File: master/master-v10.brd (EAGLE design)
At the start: 47.9 x 59.7 mm, 41 parts, among them IC1 DS1820, IC2 DS3231/SO, J1 AVR_SPI_PRG_6PTH, U2 ATMEGA640/1280/2560-A, U3 FT232RL-BASICSSOP, U4 AP1117E, U5 USD-SOCKETNEW

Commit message: arrelado problema del ftdi
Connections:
- removed net VCCIO: U3.4
- new net N$24: C8.1, C9.1, JP1.VBUS, U3.20
- new net N$25: U3.17, U3.4
- net 3.3V: no longer C8.1, C9.1, U3.20
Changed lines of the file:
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@@
 </elements>
 <signals>
-<signal name="VCCIO">
-<contactref element="U3" pad="4"/>
-</signal>
 <signal name="GND" class="1">
 <contactref element="C1" pad="2"/>
@@
 <contactref element="R6" pad="2"/>
 <contactref element="R7" pad="2"/>
-<contactref element="U3" pad="20"/>
-<contactref element="C8" pad="1"/>
-<contactref element="C9" pad="1"/>
 <contactref element="U2" pad="10"/>
 <contactref element="U2" pad="31"/>
@@
 <contactref element="R10" pad="1"/>
 <contactref element="U5" pad="4"/>
-<wire x1="22.48" y1="38.33" x2="10.795" y2="57.94" width="0" layer="19" extent="1-1"/>
-<wire x1="24.48" y1="44.83" x2="22.48" y2="38.33" width="0" layer="19" extent="1-1"/>
-<wire x1="25.48" y1="44.83" x2="24.48" y2="44.83" width="0" layer="19" extent="1-1"/>
-<wire x1="34.48" y1="44.83" x2="25.48" y2="44.83" width="0" layer="19" extent="1-1"/>
+<wire x1="34.48" y1="44.83" x2="43.21" y2="51.775" width="0" layer="19" extent="1-1"/>
+<wire x1="25.48" y1="44.83" x2="34.48" y2="44.83" width="0" layer="19" extent="1-1"/>
+<wire x1="24.48" y1="44.83" x2="25.48" y2="44.83" width="0" layer="19" extent="1-1"/>
+<wire x1="22.48" y1="38.33" x2="24.48" y2="44.83" width="0" layer="19" extent="1-1"/>
 <wire x1="38.48" y1="35.83" x2="34.48" y2="44.83" width="0" layer="19" extent="1-1"/>
-<wire x1="8.1788" y1="29.21" x2="34.48" y2="44.83" width="0" layer="19" extent="1-1"/>
+<wire x1="26.98" y1="28.83" x2="22.48" y2="38.33" width="0" layer="19" extent="1-1"/>
+<wire x1="22.9362" y1="56.515" x2="24.48" y2="44.83" width="0" layer="19" extent="1-1"/>
+<wire x1="44.45" y1="25.4" x2="38.48" y2="35.83" width="0" layer="19" extent="1-1"/>
+<wire x1="10.795" y1="57.94" x2="22.9362" y2="56.515" width="0" layer="19" extent="1-1"/>
+<wire x1="13.97" y1="27.94" x2="26.98" y2="28.83" width="0" layer="19" extent="1-1"/>
+<wire x1="8.1788" y1="29.21" x2="13.97" y2="27.94" width="0" layer="19" extent="1-1"/>
 <wire x1="1.981" y1="29.21" x2="8.1788" y2="29.21" width="0" layer="19" extent="1-1"/>
-<wire x1="26.98" y1="28.83" x2="22.48" y2="38.33" width="0" layer="19" extent="1-1"/>
-<wire x1="28.5" y1="6.88" x2="38.48" y2="35.83" width="0" layer="19" extent="1-1"/>
-<wire x1="16.356" y1="15.535" x2="1.981" y2="29.21" width="0" layer="19" extent="1-1"/>
-<wire x1="22.9362" y1="56.515" x2="16.356" y2="15.535" width="0" layer="19" extent="1-1"/>
-<wire x1="-23.51" y1="69.85" x2="22.9362" y2="56.515" width="0" layer="19" extent="1-1"/>
+<wire x1="28.5" y1="6.88" x2="26.98" y2="28.83" width="0" layer="19" extent="1-1"/>
+<wire x1="-23.51" y1="69.85" x2="10.795" y2="57.94" width="0" layer="19" extent="1-1"/>
 <wire x1="-34.94" y1="69.85" x2="-23.51" y2="69.85" width="0" layer="19" extent="1-1"/>
 <wire x1="-38.75" y1="69.85" x2="-34.94" y2="69.85" width="0" layer="19" extent="1-1"/>
@@
 <wire x1="-48.88" y1="69.85" x2="-42.56" y2="69.85" width="0" layer="19" extent="1-1"/>
 <wire x1="-52.69" y1="69.85" x2="-48.88" y2="69.85" width="0" layer="19" extent="1-1"/>
-<wire x1="-48.49" y1="64.77" x2="-48.88" y2="69.85" width="0" layer="19" extent="1-1"/>
-<wire x1="-54.34" y1="63.5" x2="-48.49" y2="64.77" width="0" layer="19" extent="1-1"/>
-<wire x1="43.21" y1="51.775" x2="-54.34" y2="63.5" width="0" layer="19" extent="1-1"/>
-<wire x1="44.45" y1="25.4" x2="-38.75" y2="69.85" width="0" layer="19" extent="1-1"/>
-<wire x1="-42.23" y1="57.15" x2="44.45" y2="25.4" width="0" layer="19" extent="1-1"/>
+<wire x1="-42.23" y1="57.15" x2="-42.56" y2="69.85" width="0" layer="19" extent="1-1"/>
 <wire x1="-47.31" y1="57.15" x2="-42.23" y2="57.15" width="0" layer="19" extent="1-1"/>
-<wire x1="-65.42" y1="69.85" x2="43.21" y2="51.775" width="0" layer="19" extent="1-1"/>
-<wire x1="13.97" y1="27.94" x2="24.48" y2="44.83" width="0" layer="19" extent="1-1"/>
+<wire x1="-65.42" y1="69.85" x2="-52.69" y2="69.85" width="0" layer="19" extent="1-1"/>
 </signal>
 <signal name="N$6">
@@
 <wire x1="-13.97" y1="62.45" x2="-14.59" y2="73.66" width="0" layer="19" extent="1-1"/>
 </signal>
+<signal name="N$24">
+<contactref element="U3" pad="20"/>
+<contactref element="C8" pad="1"/>
+<contactref element="C9" pad="1"/>
+<contactref element="JP1" pad="VBUS"/>
+<wire x1="11.1" y1="8.91" x2="16.356" y2="15.535" width="0" layer="19" extent="1-1"/>
+<wire x1="-48.49" y1="64.77" x2="16.356" y2="15.535" width="0" layer="19" extent="1-1"/>
+<wire x1="-54.34" y1="63.5" x2="-48.49" y2="64.77" width="0" layer="19" extent="1-1"/>
+</signal>
+<signal name="N$25">
+<contactref element="U3" pad="17"/>
+<contactref element="U3" pad="4"/>
+<wire x1="9.044" y1="18.785" x2="16.356" y2="13.585" width="0" layer="19" extent="1-1"/>
+</signal>
 </signals>

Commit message: avanzado temperatura y otros
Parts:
- removed IC1: DS1820, DS1820:TO-92
- added J2: TWIG-2.0-DIPD, Grove :2.0_1X4_90
- added R13: 82k, SparkFun:0402-RES
- added R14, R16: 10k, SparkFun:0402-RES
- added R15: 3.3k, SparkFun:0402-RES
- added U6: INA169, SparkFun-AnalogIC:SOT23-5
- R10: value 4k7 -> 10k
- U1: value (none) -> MCP9804; device microbuilder:SOT23-8 -> MCP9804:MSOP8
- moved U1 162.6 mm to (-106.7, -15.2), turned to 0 degrees
- moved C7 100.4 mm to (-100.3, -8.89)
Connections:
- removed net CS: U2.19, U5.2
- removed net N$14: U2.12
- removed net N$2: U2.13
- removed net SCL: IC2.16, U1.5
- removed net SDA: IC2.15, U1.6
- removed net TEMP: IC1.2, R10.2
- new net CS_SD: U2.95, U5.2
- new net N$27: U1.6
- new net RX_GPS: J2.2, U2.13
- new net SENSOR_CURRENT: C7.1, R13.2, U2.97, U6.1
- new net SENSOR_VOLT: R14.2, R15.2, U2.96
- new net TX_GPS: J2.3, U2.12
- net 3.3V: now also J2.4, R16.1, U1.8, U6.5; no longer C7.1, IC1.3, U1.4
- net GND: now also J2.1, R13.1, R15.1, U1.4, U1.5, U6.2; no longer IC1.1, U1.3, U1.8
- net MOSI: now also IC2.15, R16.2, U1.1
- net RAW: now also R14.1
- net SCK: now also IC2.16, R10.2, U1.2
- net VIN+: now also U6.3; no longer U1.1
- net VIN-: now also U6.4; no longer U1.2

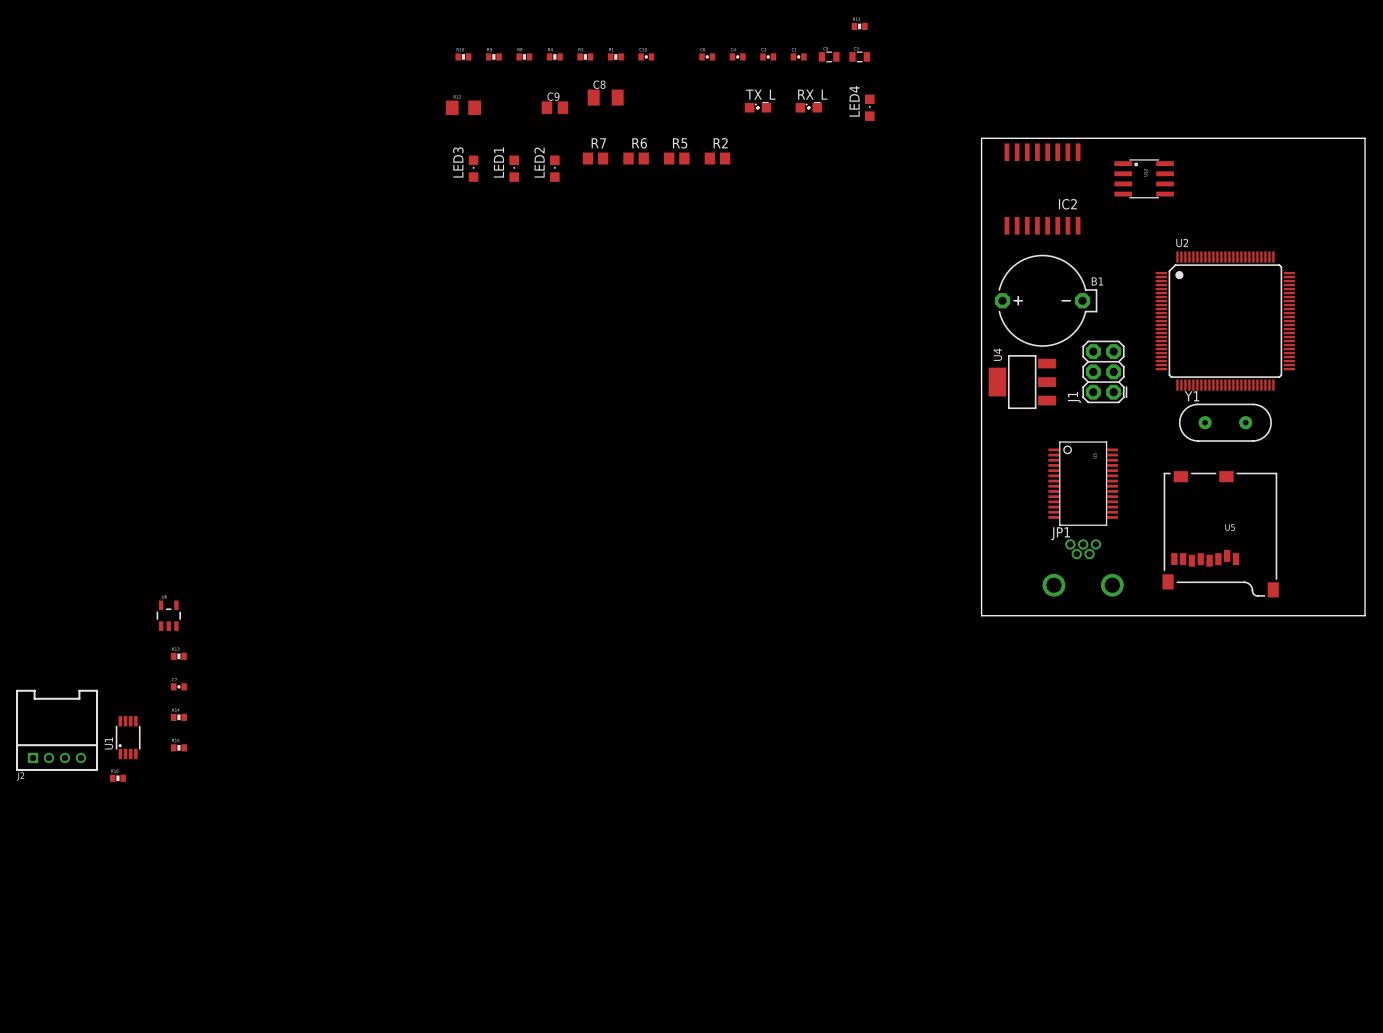
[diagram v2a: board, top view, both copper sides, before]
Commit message: agregado comunicacion
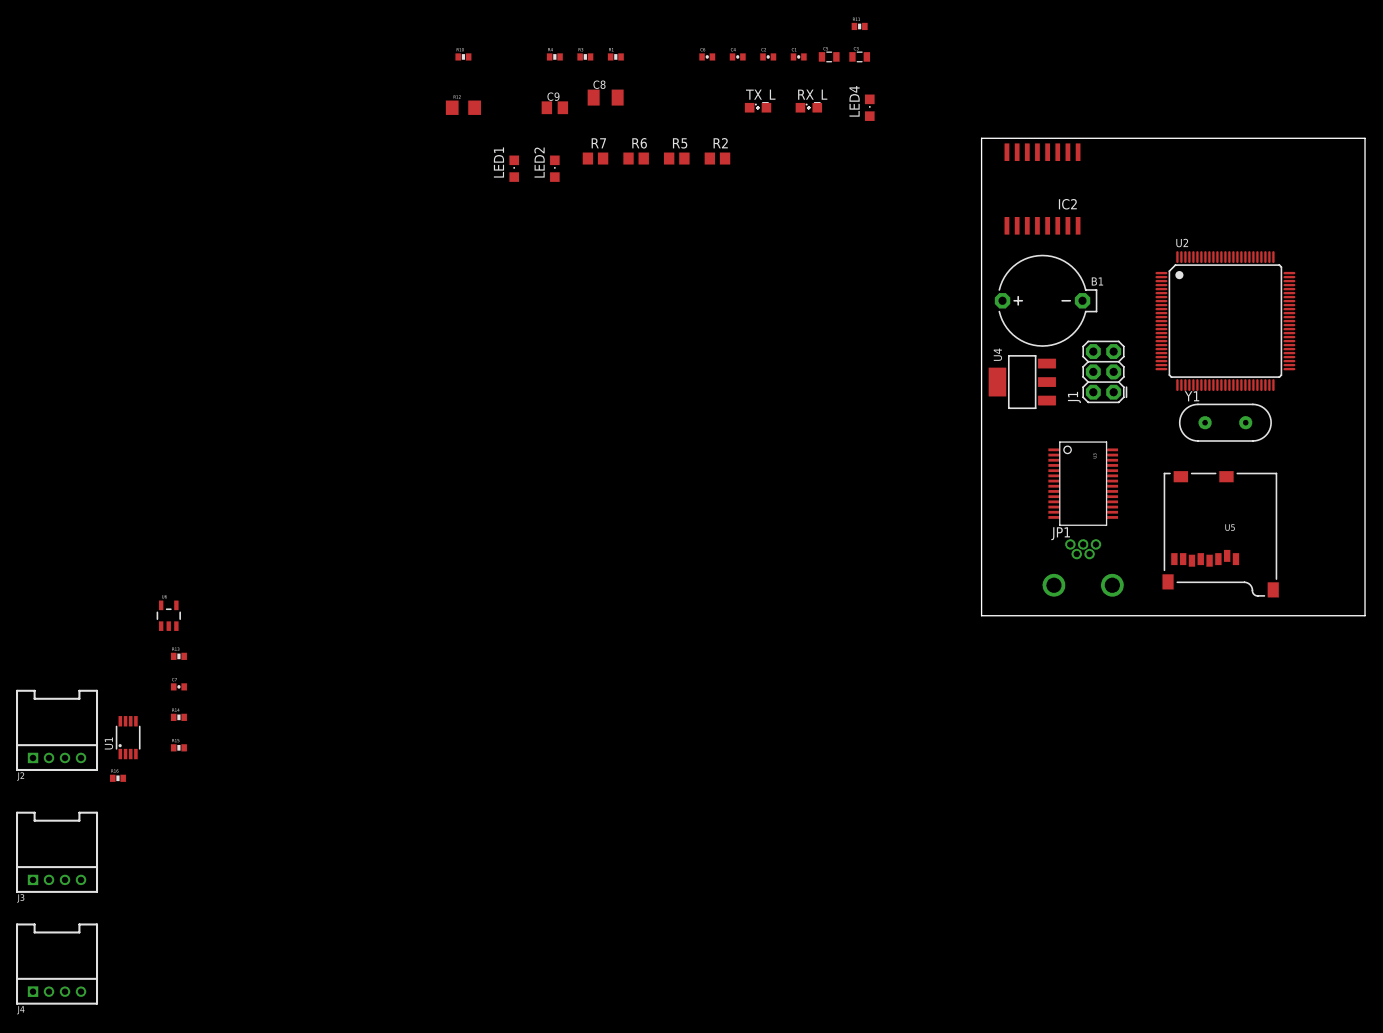
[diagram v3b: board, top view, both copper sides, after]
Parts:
- removed C10: 0.1uF, SparkFun:0402-CAP
- removed LED3: (no value), adafruit:CHIPLED_0805
- removed R8: 220, SparkFun:0402-RES
- removed R9: 1K, SparkFun:0402-RES
- removed U$2: RS485SOIC, SparkFun-DigitalIC:SO08
- added J3, J4: TWIG-2.0-DIPD, Grove :2.0_1X4_90
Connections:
- removed net A: R8.2, U$2.6
- removed net B: R8.1, U$2.7
- removed net N$15: U2.64
- removed net N$16: U2.63
- removed net N$17: U2.46
- removed net N$18: U2.45
- removed net N$20: LED3.A, R9.2
- removed net RTS: R9.1, U$2.2, U$2.3
- removed net RX-I: U$2.4
- removed net TX-O: U$2.1
- new net BT_RX: J4.2, U2.64
- new net BT_TX: J4.3, U2.63
- new net COMM_RX: J3.2, U2.46
- new net COMM_TX: J3.3, U2.45
- net 3.3V: now also J4.4; no longer C10.1, U$2.8
- net GND: now also J3.1, J4.1; no longer C10.2, LED3.C, U$2.5
- net RAW: now also J3.4
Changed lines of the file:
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@@
 <element name="JP1" library="SparkFun-Connectors" package="USB-MB-H" value="USB-MB-H" x="12.7" y="3.81" rot="R90"/>
 <element name="FRAME1" library="SparkFun-Aesthetics" package="CREATIVE_COMMONS" value="FRAME-LEDGER" x="-78.74" y="45.72"/>
-<element name="U$2" library="SparkFun-DigitalIC" package="SO08" value="RS485SOIC" x="20.32" y="54.61" rot="R270"/>
-<element name="R8" library="SparkFun" package="0402-RES" value="220" x="-57.15" y="69.85"/>
-<element name="C10" library="SparkFun" package="0402-CAP" value="0.1uF" x="-41.91" y="69.85"/>
-<element name="R9" library="SparkFun" package="0402-RES" value="1K" x="-60.96" y="69.85"/>
-<element name="LED3" library="adafruit" package="CHIPLED_0805" value="" x="-63.5" y="55.88"/>
 <element name="U4" library="v-reg" package="SOT223" value="AP1117E" x="5.08" y="29.21" rot="R90"/>
 <element name="Y1" library="SparkFun-FreqCtrl" package="HC49US" value="" x="30.48" y="24.13"/>
@@
 <element name="R16" library="SparkFun" package="0402-RES" value="10k" x="-107.95" y="-20.32"/>
 <element name="J2" library="Grove " package="2.0_1X4_90" value="TWIG-2.0-DIPD" x="-115.57" y="-17.78"/>
+<element name="J3" library="Grove " package="2.0_1X4_90" value="TWIG-2.0-DIPD" x="-115.57" y="-33.02"/>
+<element name="J4" library="Grove " package="2.0_1X4_90" value="TWIG-2.0-DIPD" x="-115.57" y="-46.99"/>
 </elements>
 <signals>
@@
 <contactref element="LED2" pad="C"/>
 <contactref element="JP1" pad="GND"/>
-<contactref element="U$2" pad="5"/>
-<contactref element="C10" pad="2"/>
-<contactref element="LED3" pad="C"/>
 <contactref element="C5" pad="2"/>
 <contactref element="C3" pad="1"/>
@@
 <contactref element="U1" pad="5"/>
 <contactref element="J2" pad="1"/>
+<contactref element="J3" pad="1"/>
+<contactref element="J4" pad="1"/>
+<wire x1="-118.57" y1="-33.02" x2="-118.57" y2="-46.99" width="0" layer="19" extent="1-1"/>
+<wire x1="-118.57" y1="-17.78" x2="-118.57" y2="-33.02" width="0" layer="19" extent="1-1"/>
 <wire x1="-107.005" y1="-13.19" x2="-118.57" y2="-17.78" width="0" layer="19" extent="1-1"/>
 <wire x1="-105.705" y1="-13.19" x2="-107.005" y2="-13.19" width="0" layer="19" extent="1-1"/>
@@
 <wire x1="-100.98" y1="-5.08" x2="-99.68" y2="-8.89" width="0" layer="19" extent="1-1"/>
 <wire x1="-101.6" y1="-1.3001" x2="-100.98" y2="-5.08" width="0" layer="19" extent="1-1"/>
-<wire x1="-63.5" y1="56.93" x2="-101.6" y2="-1.3001" width="0" layer="19" extent="1-1"/>
-<wire x1="-58.42" y1="56.93" x2="-63.5" y2="56.93" width="0" layer="19" extent="1-1"/>
+<wire x1="-58.42" y1="56.93" x2="-101.6" y2="-1.3001" width="0" layer="19" extent="1-1"/>
 <wire x1="-53.34" y1="56.93" x2="-58.42" y2="56.93" width="0" layer="19" extent="1-1"/>
 <wire x1="-52.34" y1="63.5" x2="-53.34" y2="56.93" width="0" layer="19" extent="1-1"/>
 <wire x1="-45.49" y1="64.77" x2="-52.34" y2="63.5" width="0" layer="19" extent="1-1"/>
-<wire x1="-41.26" y1="69.85" x2="-45.49" y2="64.77" width="0" layer="19" extent="1-1"/>
-<wire x1="-29.83" y1="69.85" x2="-41.26" y2="69.85" width="0" layer="19" extent="1-1"/>
+<wire x1="-29.83" y1="69.85" x2="-45.49" y2="64.77" width="0" layer="19" extent="1-1"/>
 <wire x1="-22.21" y1="69.85" x2="-29.83" y2="69.85" width="0" layer="19" extent="1-1"/>
 <wire x1="-18.15" y1="69.85" x2="-22.21" y2="69.85" width="0" layer="19" extent="1-1"/>
@@
 <wire x1="5.715" y1="57.94" x2="4.445" y2="57.94" width="0" layer="19" extent="1-1"/>
 <wire x1="6.985" y1="57.94" x2="5.715" y2="57.94" width="0" layer="19" extent="1-1"/>
-<wire x1="22.9362" y1="52.705" x2="6.985" y2="57.94" width="0" layer="19" extent="1-1"/>
-<wire x1="24.98" y1="44.83" x2="22.9362" y2="52.705" width="0" layer="19" extent="1-1"/>
+<wire x1="24.98" y1="44.83" x2="6.985" y2="57.94" width="0" layer="19" extent="1-1"/>
 <wire x1="22.48" y1="37.83" x2="24.98" y2="44.83" width="0" layer="19" extent="1-1"/>
 <wire x1="33.98" y1="44.83" x2="24.98" y2="44.83" width="0" layer="19" extent="1-1"/>
@@
 <contactref element="U4" pad="3"/>
 <contactref element="R14" pad="1"/>
+<contactref element="J3" pad="4"/>
+<wire x1="-100.98" y1="-12.7" x2="-112.57" y2="-33.02" width="0" layer="19" extent="1-1"/>
 <wire x1="-31.13" y1="69.85" x2="-100.98" y2="-12.7" width="0" layer="19" extent="1-1"/>
 <wire x1="8.1788" y1="31.5214" x2="-31.13" y2="69.85" width="0" layer="19" extent="1-1"/>
@@
 <contactref element="U2" pad="98"/>
 <contactref element="R3" pad="2"/>
-<contactref element="U$2" pad="8"/>
-<contactref element="C10" pad="1"/>
 <contactref element="U5" pad="4"/>
 <contactref element="U6" pad="5"/>
@@
 <contactref element="R10" pad="1"/>
 <contactref element="J2" pad="4"/>
-<wire x1="-108.6" y1="-20.32" x2="-112.57" y2="-17.78" width="0" layer="19" extent="1-1"/>
+<contactref element="J4" pad="4"/>
+<wire x1="-108.6" y1="-20.32" x2="-112.57" y2="-46.99" width="0" layer="19" extent="1-1"/>
+<wire x1="-112.57" y1="-17.78" x2="-108.6" y2="-20.32" width="0" layer="19" extent="1-1"/>
 <wire x1="-107.655" y1="-13.19" x2="-112.57" y2="-17.78" width="0" layer="19" extent="1-1"/>
 <wire x1="-102.55" y1="1.3001" x2="-107.655" y2="-13.19" width="0" layer="19" extent="1-1"/>
@@
 <wire x1="-52.69" y1="69.85" x2="-65.42" y2="69.85" width="0" layer="19" extent="1-1"/>
 <wire x1="-48.88" y1="69.85" x2="-52.69" y2="69.85" width="0" layer="19" extent="1-1"/>
-<wire x1="-42.56" y1="69.85" x2="-48.88" y2="69.85" width="0" layer="19" extent="1-1"/>
-<wire x1="-34.94" y1="69.85" x2="-42.56" y2="69.85" width="0" layer="19" extent="1-1"/>
+<wire x1="-47.31" y1="57.15" x2="-48.88" y2="69.85" width="0" layer="19" extent="1-1"/>
+<wire x1="-42.23" y1="57.15" x2="-47.31" y2="57.15" width="0" layer="19" extent="1-1"/>
+<wire x1="-34.94" y1="69.85" x2="-48.88" y2="69.85" width="0" layer="19" extent="1-1"/>
 <wire x1="-23.51" y1="69.85" x2="-34.94" y2="69.85" width="0" layer="19" extent="1-1"/>
-<wire x1="-42.23" y1="57.15" x2="-42.56" y2="69.85" width="0" layer="19" extent="1-1"/>
-<wire x1="-47.31" y1="57.15" x2="-42.23" y2="57.15" width="0" layer="19" extent="1-1"/>
 <wire x1="10.795" y1="57.94" x2="-23.51" y2="69.85" width="0" layer="19" extent="1-1"/>
-<wire x1="22.9362" y1="56.515" x2="10.795" y2="57.94" width="0" layer="19" extent="1-1"/>
-<wire x1="24.48" y1="44.83" x2="22.9362" y2="56.515" width="0" layer="19" extent="1-1"/>
+<wire x1="24.48" y1="44.83" x2="10.795" y2="57.94" width="0" layer="19" extent="1-1"/>
 <wire x1="25.48" y1="44.83" x2="24.48" y2="44.83" width="0" layer="19" extent="1-1"/>
 <wire x1="22.48" y1="38.33" x2="24.48" y2="44.83" width="0" layer="19" extent="1-1"/>
@@
 <wire x1="-37.15" y1="57.15" x2="22.48" y2="41.83" width="0" layer="19" extent="1-1"/>
 </signal>
-<signal name="N$15">
+<signal name="BT_RX">
 <contactref element="U2" pad="64"/>
-</signal>
-<signal name="N$16">
+<contactref element="J4" pad="2"/>
+<wire x1="38.48" y1="37.33" x2="-116.57" y2="-46.99" width="0" layer="19" extent="1-1"/>
+</signal>
+<signal name="BT_TX">
 <contactref element="U2" pad="63"/>
-</signal>
-<signal name="N$17">
-<contactref element="U2" pad="46"/>
-</signal>
-<signal name="N$18">
-<contactref element="U2" pad="45"/>
+<contactref element="J4" pad="3"/>
+<wire x1="38.48" y1="36.83" x2="-114.57" y2="-46.99" width="0" layer="19" extent="1-1"/>
 </signal>
 <signal name="N$5">
@@
 <contactref element="JP1" pad="D-"/>
 <wire x1="11.9" y1="7.71" x2="16.356" y2="12.935" width="0" layer="19" extent="1-1"/>
-</signal>
-<signal name="TX-O">
-<contactref element="U$2" pad="1"/>
-</signal>
-<signal name="RTS">
-<contactref element="U$2" pad="2"/>
-<contactref element="U$2" pad="3"/>
-<contactref element="R9" pad="1"/>
-<wire x1="17.7038" y1="55.245" x2="17.7038" y2="53.975" width="0" layer="19" extent="1-1"/>
-<wire x1="-61.61" y1="69.85" x2="17.7038" y2="55.245" width="0" layer="19" extent="1-1"/>
-</signal>
-<signal name="RX-I">
-<contactref element="U$2" pad="4"/>
-</signal>
-<signal name="B">
-<contactref element="U$2" pad="7"/>
-<contactref element="R8" pad="1"/>
-<wire x1="-57.8" y1="69.85" x2="22.9362" y2="55.245" width="0" layer="19" extent="1-1"/>
-</signal>
-<signal name="A">
-<contactref element="U$2" pad="6"/>
-<contactref element="R8" pad="2"/>
-<wire x1="-56.5" y1="69.85" x2="22.9362" y2="53.975" width="0" layer="19" extent="1-1"/>
-</signal>
-<signal name="N$20">
-<contactref element="R9" pad="2"/>
-<contactref element="LED3" pad="A"/>
-<wire x1="-63.5" y1="54.83" x2="-60.31" y2="69.85" width="0" layer="19" extent="1-1"/>
 </signal>
 <signal name="N$21">
@@
 <wire x1="22.48" y1="37.33" x2="-114.57" y2="-17.78" width="0" layer="19" extent="1-1"/>
 </signal>
+<signal name="COMM_RX">
+<contactref element="J3" pad="2"/>
+<contactref element="U2" pad="46"/>
+<wire x1="34.48" y1="28.83" x2="-116.57" y2="-33.02" width="0" layer="19" extent="1-1"/>
+</signal>
+<signal name="COMM_TX">
+<contactref element="J3" pad="3"/>
+<contactref element="U2" pad="45"/>
+<wire x1="33.98" y1="28.83" x2="-114.57" y2="-33.02" width="0" layer="19" extent="1-1"/>
+</signal>
 </signals>
